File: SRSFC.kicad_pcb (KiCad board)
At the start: 4 copper layers, 52.6 x 33.8 mm, 56 parts, among them J1 SWD_interface, J2 POWER, J3 SERVO1, J4 SERVO2, J5 SERVO3, J6 SERVO4, J7 SERVO5, J8 IBUS_RX, X1 25MHz

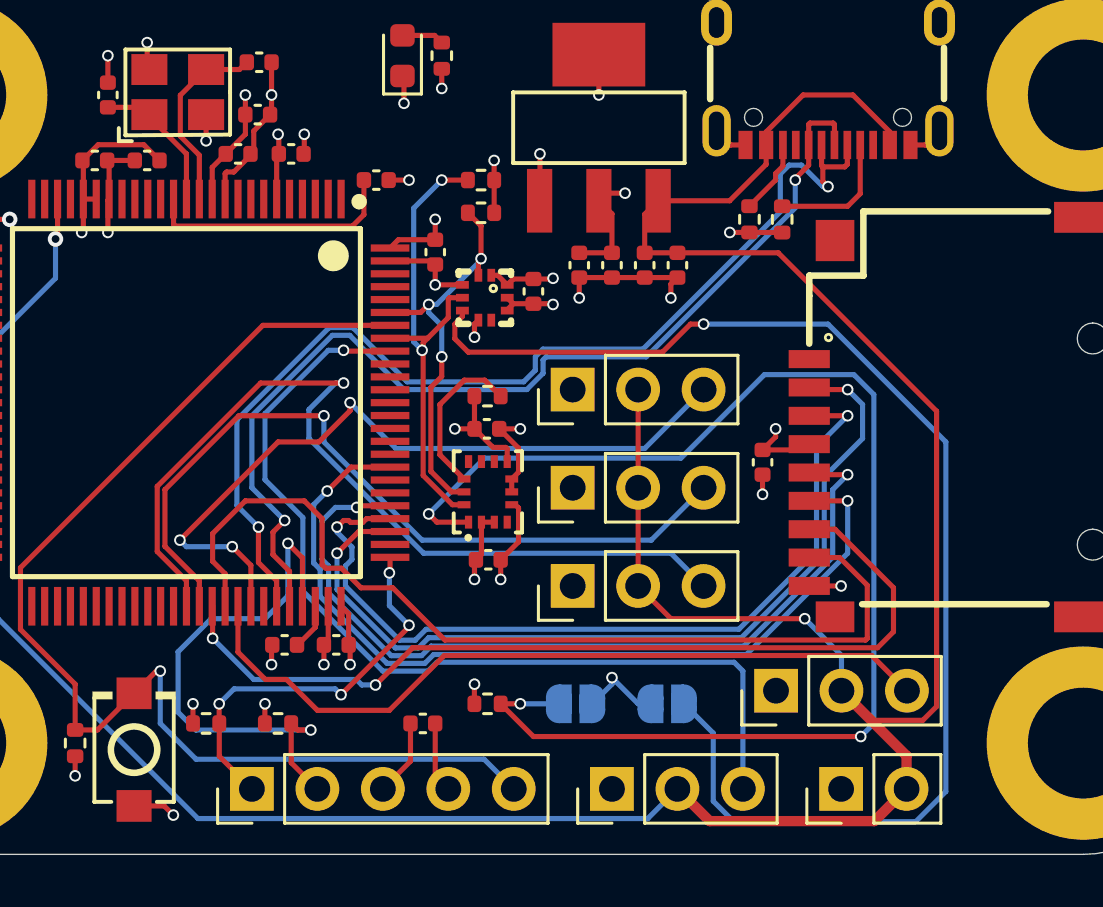
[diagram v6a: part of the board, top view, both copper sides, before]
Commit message: changed sensors from i2c to SPI, fixed silkscreen
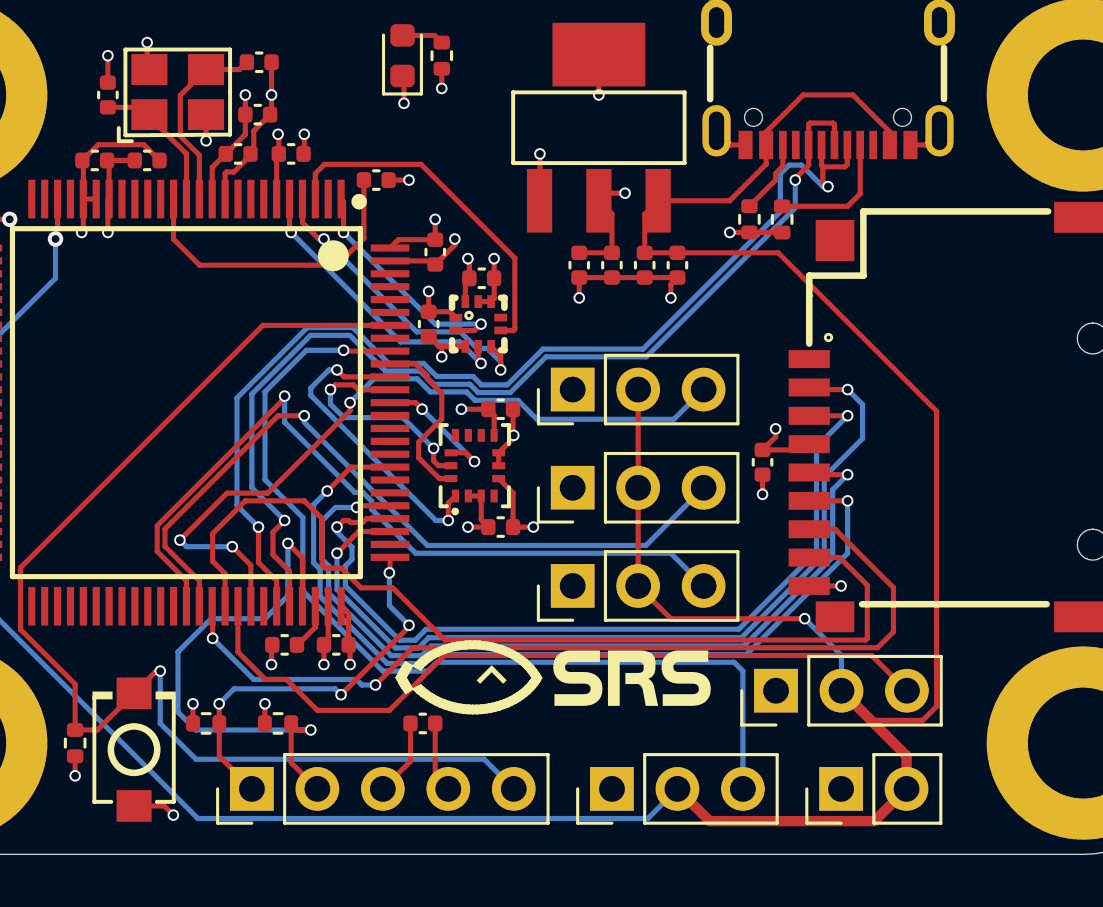
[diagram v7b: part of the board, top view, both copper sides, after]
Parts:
- removed JP1, JP2: address_select, Jumper:SolderJumper-2_P1.3mm_Open_RoundedPad1.0x1.5mm
- removed R10, R9: 4.7k, Resistor_SMD:R_0402_1005Metric
- removed R7, R8: 10k, Resistor_SMD:R_0402_1005Metric
- added C17: 100nF, Capacitor_SMD:C_0402_1005Metric, F.Cu at (141.5, 94.7)
- moved C28 2.07 mm to (143.5, 93.0), turned to 0 degrees
- moved C16 1.36 mm to (144.3, 102.6), turned to 0 degrees
- moved U2 1.14 mm to (143.3, 100.2)
- moved U6 1.05 mm to (143.4, 94.7), turned to 90 degrees
- moved C15 0.93 mm to (144.3, 98.0), turned to 0 degrees
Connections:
- C15 pad 1: GND -> +3.3V
- C15 pad 2: +3.3V -> GND
- C16 pad 1: +3.3V -> GND
- C16 pad 2: GND -> +3.3V
- U1 pad 1: unconnected-(U1-PE2-Pad1) -> /SPI_SCK_BMP
- U1 pad 3: unconnected-(U1-PE4-Pad3) -> /SPI_CS_BMP
- U1 pad 4: unconnected-(U1-PE5-Pad4) -> /SPI_MISO_BMP
- U1 pad 5: unconnected-(U1-PE6-Pad5) -> /SPI_MOSI_BMP
- U1 pad 88: unconnected-(U1-PD7-Pad88) -> /SPI_CS_LSM
- U1 pad 89: unconnected-(U1-PB3-Pad89) -> /SPI_SCK_LSM
- U1 pad 90: unconnected-(U1-PB4-Pad90) -> /SPI_MISO_LSM
- U1 pad 91: unconnected-(U1-PB5-Pad91) -> /SPI_MOSI_LSM
- U1 pad 93: /bmp_sda -> unconnected-(U1-PB7-Pad93)
- U1 pad 95: /bmp_scl -> unconnected-(U1-PB8-Pad95)
- U2 pad 1: Net-(JP1-A) -> /SPI_MISO_LSM
- U2 pad 12: Net-(U2-CS) -> /SPI_CS_LSM
- U2 pad 13: /bmp_scl -> /SPI_SCK_LSM
- U2 pad 14: /bmp_sda -> /SPI_MOSI_LSM
- U6 pad 2: /bmp_scl -> /SPI_SCK_BMP
- U6 pad 4: /bmp_sda -> /SPI_MOSI_BMP
- U6 pad 5: Net-(JP2-A) -> /SPI_MISO_BMP
- U6 pad 6: +3.3V -> /SPI_CS_BMP
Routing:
- net Net-(JP1-A): track 51.7 -> 0.00 mm, vias 3 -> 0
- net Net-(JP2-A): track 50.5 -> 0.00 mm, vias 1 -> 0
- net /bmp_sda: track 19.6 -> 0.00 mm, vias 2 -> 0
- net /bmp_scl: track 15.6 -> 0.00 mm, vias 3 -> 0
- net /SPI_CS_BMP: track 0.00 -> 13.7 mm
- net /SPI_MISO_BMP: track 0.00 -> 12.2 mm, vias 0 -> 2
- net /SPI_MISO_LSM: track 0.00 -> 12.2 mm, vias 0 -> 2
- net /SPI_MOSI_BMP: track 0.00 -> 11.5 mm, vias 0 -> 2
- net /SPI_SCK_BMP: track 0.00 -> 9.22 mm, vias 0 -> 2
- net /SPI_SCK_LSM: track 0.00 -> 8.99 mm, vias 0 -> 2
- net /SPI_MOSI_LSM: track 0.00 -> 7.01 mm
- net Net-(U2-CS): track 6.28 -> 0.00 mm
- net /SPI_CS_LSM: track 0.00 -> 5.28 mm, vias 0 -> 2
- net +3.3V: track 54.8 -> 49.8 mm, vias 19 -> 17
- net /servo_3: track 34.6 -> 30.8 mm
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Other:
- board text added: "POLARIS"
- board text removed: "FC V1.0"
- board text removed: "SRS"

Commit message: final commit before ordering
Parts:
- R2: value 220 -> 100
- moved C27 0.45 mm to (154.4, 100.6)
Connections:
- CARD1 pad 1: unconnected-(CARD1-DAT2-Pad1) -> /SDIO_D2
- CARD1 pad 10: unconnected-(CARD1-Pad10) -> GND
- CARD1 pad 11: unconnected-(CARD1-Pad11) -> GND
- CARD1 pad 12: unconnected-(CARD1-Pad12) -> GND
- CARD1 pad 13: unconnected-(CARD1-Pad13) -> GND
- CARD1 pad 2: /SDIO_D2 -> /SDIO_D3
- CARD1 pad 3: /SDIO_D3 -> /SDIO_CMD
- CARD1 pad 6: /SDIO_CMD -> GND
- CARD1 pad CD: GND -> /SD_CD
- U1 pad 77: unconnected-(U1-PA15-Pad77) -> /SD_CD
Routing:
- net /SD_CD: track 0.00 -> 17.4 mm, vias 0 -> 2
- net GND: track 55.6 -> 63.2 mm, vias 26 -> 29
- net /SDIO_SCK: track 32.9 -> 37.1 mm
- net /SDIO_CMD: track 34.1 -> 37.3 mm
- net /SDIO_D2: track 33.9 -> 35.0 mm
- net /SDIO_D3: track 32.7 -> 33.7 mm
- net /SDIO_D0: track 35.2 -> 34.4 mm
